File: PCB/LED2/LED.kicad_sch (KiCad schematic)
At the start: 29 parts, among them J1 Conn_01x03, J2 USB-C, U1 ESP32-PICO-MINI-02, U2 QR, U3 CH340X, U4 Barcode, U5 MD8942

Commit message: Started tracking
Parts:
- removed C4 (x2): 100nF, RevK:C_0402, symbol Device:C
- removed U1: ESP32-PICO-MINI-02, RevK:ESP32-PICO-MINI-02, symbol RevK:ESP32-PICO-MINI-02
- removed U2: QR, RevK:QR-LED, symbol RevK:QR
- removed U3: CH340X, RevK:CH340X, symbol RevK:CH340X
- added C2: 22uF, RevK:C_0402, symbol Device:C
- added C3: 1uF, RevK:C_0402, symbol Device:C
- added J2: Shelly, RevK:Shelly, symbol RevK:Shelly
- added U2: ESP32-S3-MINI-1, RevK:ESP32-S3-MINI-1, symbol RevK:ESP32-S3-MINI-1-N4R2
- C1: value 1uF -> 100nF
- J1: now left out of the parts list
- R1: value 10k -> 10K
- R10: value 40k2 -> 39k2
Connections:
- net +3V3: now also C1.1, C2.1, J2.3 (3V3), U2.3 (3V3)
- net B: now also U2.15 (GPIO11)
- net D+: now also U2.24 (GPIO20)
- net D-: now also U2.23 (GPIO19)
- net G: now also U2.13 (GPIO9)
- net GND: now also C1.2, C2.2, C3.2, J2.1 (GND), U2.1 (GND), U2.2 (GND), U2.42 (GND), U2.43 (GND), U2.46 (GND), U2.47 (GND), U2.48 (GND), U2.49 (GND), U2.50 (GND), U2.51 (GND), U2.52 (GND), U2.53 (GND), U2.54 (GND), U2.55 (GND), U2.56 (GND), U2.57 (GND), U2.58 (GND), U2.59 (GND), U2.60 (GND), U2.61 (GND), U2.62 (GND), U2.63 (GND), U2.64 (GND), U2.65 (GND); no longer C1.1
- net R: now also U2.14 (GPIO10)
- net EN: no longer names the net of R1.2
- net EN: now also C3.1, U2.45 (EN); no longer C1.2
- new net: J2.5 (Tx), U2.39 (GPIO43)
- new net: J2.2 (0), U2.4 (GPIO0)
- new net: J2.4 (Rx), U2.40 (GPIO44)
- no-connect marks 20 -> 1

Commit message: New S3
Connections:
- net LED: now also U2.12 (GPIO8)
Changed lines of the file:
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@@
+    )
+  )
+  (global_label "LED" (shape output) (at 35.56 68.58 180) (fields_autoplaced)
+    (effects (font (size 1.27 1.27)) (justify right))
+    (property "Intersheetrefs" "${INTERSHEET_REFS}" (at 29.7819 68.58 0)
+      (effects (font (size 1.27 1.27)) (justify right) hide)
     )
   )

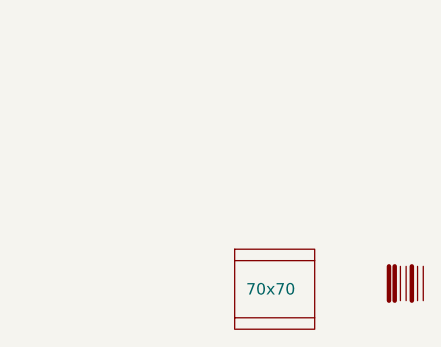
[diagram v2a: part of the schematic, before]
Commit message: LED input
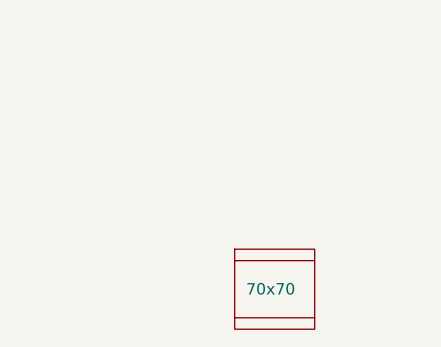
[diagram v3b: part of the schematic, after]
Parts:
- removed U4: Barcode, RevK:EAN-5060634238090, symbol RevK:Barcode
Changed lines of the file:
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@@
-    )
-  )
-  (symbol (lib_id "RevK:Barcode") (at 274.32 172.72 0) (unit 1)
-    (in_bom no) (on_board yes) (dnp no) (fields_autoplaced)
-    (property "Reference" "U4" (at 274.32 175.895 0)
-      (effects (font (size 1.27 1.27)) hide)
-    )
-    (property "Value" "Barcode" (at 274.32 177.8 0)
-      (effects (font (size 1.27 1.27)) hide)
-    )
-    (property "Footprint" "RevK:EAN-5060634238090" (at 273.685 173.355 0)
-      (effects (font (size 1.27 1.27)) hide)
-    )
-    (property "Datasheet" "" (at 273.685 173.355 0)
-      (effects (font (size 1.27 1.27)) hide)
-    )
-    (property "Note" "Non part, PCB printed" (at 274.32 167.005 0)
-      (effects (font (size 1.27 1.27)) hide)
-    )
-    (instances
-      (project "LED"
-        (path "/46c350bb-7de4-4e81-aafd-4af55e37aab0"
-          (reference "U4") (unit 1)
-        )
-      )
     )
   )

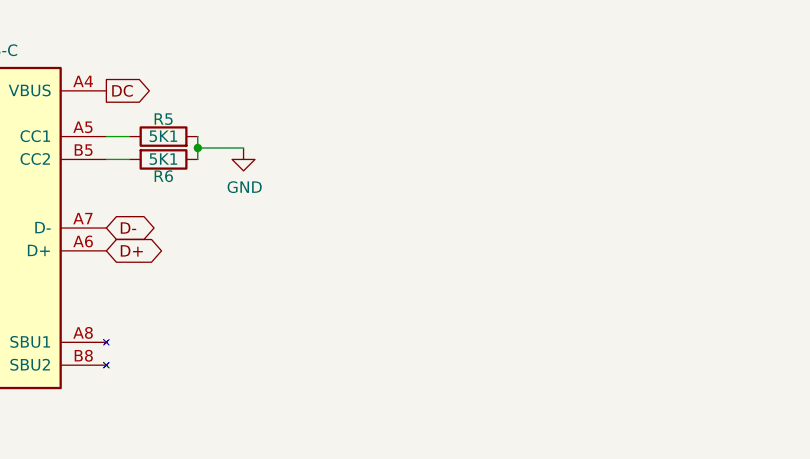
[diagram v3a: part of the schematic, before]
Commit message: Clean up, allow in panel USB prog.
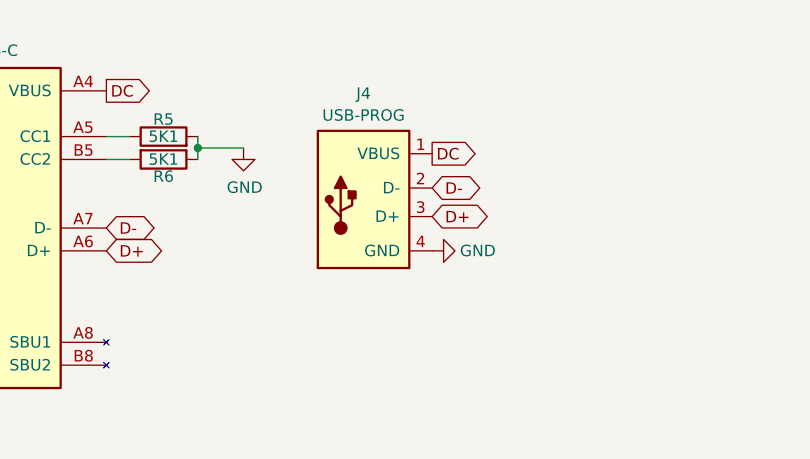
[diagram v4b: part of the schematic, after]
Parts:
- added J4: USB-PROG, RevK:USB-PROG, symbol RevK:USB-PROG
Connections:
- net D+: now also J4.3 (D+)
- net D-: now also J4.2 (D-)
- net DC: now also J4.1 (VBUS)
- net GND: now also J4.4 (GND)
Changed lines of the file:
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@@
+    )
+  )
+  (global_label "D-" (shape bidirectional) (at 209.55 37.465 0) (fields_autoplaced)
+    (effects (font (size 1.27 1.27)) (justify left))
+    (property "Intersheetrefs" "${INTERSHEET_REFS}" (at 215.5965 37.465 0)
+      (effects (font (size 1.27 1.27)) (justify left) hide)
     )
   )
@@
     )
   )
+  (global_label "DC" (shape input) (at 133.35 87.63 180) (fields_autoplaced)
+    (effects (font (size 1.27 1.27)) (justify right))
+    (property "Intersheetrefs" "${INTERSHEET_REFS}" (at 128.5584 87.63 0)
+      (effects (font (size 1.27 1.27)) (justify right) hide)
+    )
+  )
+  (global_label "DC" (shape output) (at 173.355 26.67 0) (fields_autoplaced)
+    (effects (font (size 1.27 1.27)) (justify left))
+    (property "Intersheetrefs" "${INTERSHEET_REFS}" (at 178.1466 26.67 0)
+      (effects (font (size 1.27 1.27)) (justify left) hide)
+    )
+  )
+  (global_label "R" (shape output) (at 35.56 73.66 180) (fields_autoplaced)
+    (effects (font (size 1.27 1.27)) (justify right))
+    (property "Intersheetrefs" "${INTERSHEET_REFS}" (at 31.959 73.66 0)
+      (effects (font (size 1.27 1.27)) (justify right) hide)
+    )
+  )
+  (global_label "DC" (shape input) (at 167.005 83.185 180) (fields_autoplaced)
+    (effects (font (size 1.27 1.27)) (justify right))
+    (property "Intersheetrefs" "${INTERSHEET_REFS}" (at 162.134 83.185 0)
+      (effects (font (size 1.27 1.27)) (justify right) hide)
+    )
+  )
+  (global_label "LED" (shape input) (at 113.03 90.17 180) (fields_autoplaced)
+    (effects (font (size 1.27 1.27)) (justify right))
+    (property "Intersheetrefs" "${INTERSHEET_REFS}" (at 107.2587 90.0906 0)
+      (effects (font (size 1.27 1.27)) (justify right) hide)
+    )
+  )
   (global_label "D-" (shape bidirectional) (at 173.355 41.91 0) (fields_autoplaced)
     (effects (font (size 1.27 1.27)) (justify left))
@@
     )
   )
-  (global_label "DC" (shape input) (at 133.35 87.63 180) (fields_autoplaced)
-    (effects (font (size 1.27 1.27)) (justify right))
-    (property "Intersheetrefs" "${INTERSHEET_REFS}" (at 128.5584 87.63 0)
-      (effects (font (size 1.27 1.27)) (justify right) hide)
-    )
-  )
-  (global_label "DC" (shape output) (at 173.355 26.67 0) (fields_autoplaced)
-    (effects (font (size 1.27 1.27)) (justify left))
-    (property "Intersheetrefs" "${INTERSHEET_REFS}" (at 178.1466 26.67 0)
-      (effects (font (size 1.27 1.27)) (justify left) hide)
-    )
-  )
-  (global_label "R" (shape output) (at 35.56 73.66 180) (fields_autoplaced)
-    (effects (font (size 1.27 1.27)) (justify right))
-    (property "Intersheetrefs" "${INTERSHEET_REFS}" (at 31.959 73.66 0)
-      (effects (font (size 1.27 1.27)) (justify right) hide)
-    )
-  )
-  (global_label "DC" (shape input) (at 167.005 83.185 180) (fields_autoplaced)
-    (effects (font (size 1.27 1.27)) (justify right))
-    (property "Intersheetrefs" "${INTERSHEET_REFS}" (at 162.134 83.185 0)
-      (effects (font (size 1.27 1.27)) (justify right) hide)
-    )
-  )
-  (global_label "LED" (shape input) (at 113.03 90.17 180) (fields_autoplaced)
-    (effects (font (size 1.27 1.27)) (justify right))
-    (property "Intersheetrefs" "${INTERSHEET_REFS}" (at 107.2587 90.0906 0)
-      (effects (font (size 1.27 1.27)) (justify right) hide)
-    )
-  )
   (global_label "G" (shape input) (at 100.33 41.275 180) (fields_autoplaced)
     (effects (font (size 1.27 1.27)) (justify right))
@@
     (property "Intersheetrefs" "${INTERSHEET_REFS}" (at 29.5135 96.52 0)
       (effects (font (size 1.27 1.27)) (justify right) hide)
+    )
+  )
+  (global_label "D+" (shape bidirectional) (at 209.55 40.64 0) (fields_autoplaced)
+    (effects (font (size 1.27 1.27)) (justify left))
+    (property "Intersheetrefs" "${INTERSHEET_REFS}" (at 215.5965 40.64 0)
+      (effects (font (size 1.27 1.27)) (justify left) hide)
+    )
+  )
+  (global_label "DC" (shape output) (at 209.55 33.655 0) (fields_autoplaced)
+    (effects (font (size 1.27 1.27)) (justify left))
+    (property "Intersheetrefs" "${INTERSHEET_REFS}" (at 214.3416 33.655 0)
+      (effects (font (size 1.27 1.27)) (justify left) hide)
     )
   )
@@
     )
   )
+  (symbol (lib_id "RevK:USB-PROG") (at 201.93 38.735 0) (unit 1)
+    (in_bom yes) (on_board yes) (dnp no) (fields_autoplaced)
+    (property "Reference" "J4" (at 201.93 26.9707 0)
+      (effects (font (size 1.27 1.27)))
+    )
+    (property "Value" "USB-PROG" (at 201.93 29.3949 0)
+      (effects (font (size 1.27 1.27)))
+    )
+    (property "Footprint" "RevK:USB-PROG" (at 205.74 40.005 0)
+      (effects (font (size 1.27 1.27)) hide)
+    )
+    (property "Datasheet" " ~" (at 205.74 40.005 0)
+      (effects (font (size 1.27 1.27)) hide)
+    )
+    (pin "1")
+    (pin "2")
+    (pin "3")
+    (pin "4")
+    (instances
+      (project "LED"
+        (path "/46c350bb-7de4-4e81-aafd-4af55e37aab0"
+          (reference "J4") (unit 1)
+        )
+      )
+    )
+  )
   (symbol (lib_id "Device:C") (at 53.975 31.115 0) (unit 1)
     (in_bom yes) (on_board yes) (dnp no) (fields_autoplaced)
@@
         )
       )
+    )
+  )
+  (symbol (lib_id "power:GND") (at 209.55 44.45 90) (unit 1)
+    (in_bom yes) (on_board yes) (dnp no)
+    (property "Reference" "#PWR01" (at 215.9 44.45 0)
+      (effects (font (size 1.27 1.27)) hide)
+    )
+    (property "Value" "GND" (at 214.63 44.45 90)
+      (effects (font (size 1.27 1.27)))
+    )
+    (property "Footprint" "" (at 209.55 44.45 0)
+      (effects (font (size 1.27 1.27)) hide)
+    )
+    (property "Datasheet" "" (at 209.55 44.45 0)
+      (effects (font (size 1.27 1.27)) hide)
+    )
+    (pin "1")
+    (instances
+      (project "LED"
+        (path "/46c350bb-7de4-4e81-aafd-4af55e37aab0"
+          (reference "#PWR01") (unit 1)
+        )
+      )

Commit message: New Reg
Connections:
- net GND: now also U2.10 (GPIO6), U2.11 (GPIO7), U2.5 (GPIO1), U2.6 (GPIO2), U2.8 (GPIO4), U2.9 (GPIO5)
- no-connect marks 1 -> 24
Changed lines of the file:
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@@
   (junction (at 80.01 105.41) (diameter 0) (color 0 0 0 0)
   )
+  (no_connect (at 66.04 96.52))
+  (no_connect (at 66.04 76.2))
+  (no_connect (at 66.04 101.6))
+  (no_connect (at 66.04 93.98))
+  (no_connect (at 35.56 91.44))
+  (no_connect (at 35.56 55.88))
+  (no_connect (at 35.56 101.6))
+  (no_connect (at 66.04 81.28))
+  (no_connect (at 35.56 88.9))
   (no_connect (at 167.005 93.98))
+  (no_connect (at 35.56 81.28))
+  (no_connect (at 66.04 86.36))
+  (no_connect (at 35.56 93.98))
+  (no_connect (at 66.04 78.74))
+  (no_connect (at 35.56 78.74))
+  (no_connect (at 66.04 73.66))
+  (no_connect (at 66.04 71.12))
+  (no_connect (at 66.04 66.04))
+  (no_connect (at 66.04 83.82))
+  (no_connect (at 35.56 83.82))
+  (no_connect (at 66.04 99.06))
+  (no_connect (at 66.04 88.9))
+  (no_connect (at 66.04 68.58))
+  (no_connect (at 35.56 86.36))
   (wire (pts (xy 183.515 33.02) (xy 183.515 34.29))
     (stroke (width 0) (type default))
@@
     )
   )
+  (symbol (lib_id "power:GND") (at 35.56 58.42 270) (unit 1)
+    (in_bom yes) (on_board yes) (dnp no) (fields_autoplaced)
+    (property "Reference" "#PWR0105" (at 29.21 58.42 0)
+      (effects (font (size 1.27 1.27)) hide)
+    )
+    (property "Value" "GND" (at 32.3851 58.42 90)
+      (effects (font (size 1.27 1.27)) (justify right))
+    )
+    (property "Footprint" "" (at 35.56 58.42 0)
+      (effects (font (size 1.27 1.27)) hide)
+    )
+    (property "Datasheet" "" (at 35.56 58.42 0)
+      (effects (font (size 1.27 1.27)) hide)
+    )
+    (pin "1")
+    (instances
+      (project "GenericS3"
+        (path "/2d210a96-f81f-42a9-8bf4-1b43c11086f3"
+          (reference "#PWR0105") (unit 1)
+        )
+      )
+      (project "LED"
+        (path "/46c350bb-7de4-4e81-aafd-4af55e37aab0"
+          (reference "#PWR04") (unit 1)
+        )
+      )
+    )
+  )
   (symbol (lib_id "RevK:Hidden") (at 199.39 92.075 0) (unit 1)
     (in_bom yes) (on_board yes) (dnp no)
@@
         (path "/46c350bb-7de4-4e81-aafd-4af55e37aab0"
           (reference "#PWR022") (unit 1)
+        )
+      )
+    )
+  )
+  (symbol (lib_id "power:GND") (at 35.56 63.5 270) (unit 1)
+    (in_bom yes) (on_board yes) (dnp no) (fields_autoplaced)
+    (property "Reference" "#PWR0105" (at 29.21 63.5 0)
+      (effects (font (size 1.27 1.27)) hide)
+    )
+    (property "Value" "GND" (at 32.3851 63.5 90)
+      (effects (font (size 1.27 1.27)) (justify right))
+    )
+    (property "Footprint" "" (at 35.56 63.5 0)
+      (effects (font (size 1.27 1.27)) hide)
+    )
+    (property "Datasheet" "" (at 35.56 63.5 0)
+      (effects (font (size 1.27 1.27)) hide)
+    )
+    (pin "1")
+    (instances
+      (project "GenericS3"
+        (path "/2d210a96-f81f-42a9-8bf4-1b43c11086f3"
+          (reference "#PWR0105") (unit 1)
+        )
+      )
+      (project "LED"
+        (path "/46c350bb-7de4-4e81-aafd-4af55e37aab0"
+          (reference "#PWR06") (unit 1)
         )
       )
@@
     )
   )
+  (symbol (lib_id "power:GND") (at 35.56 53.34 270) (unit 1)
+    (in_bom yes) (on_board yes) (dnp no) (fields_autoplaced)
+    (property "Reference" "#PWR0105" (at 29.21 53.34 0)
+      (effects (font (size 1.27 1.27)) hide)
+    )
+    (property "Value" "GND" (at 32.3851 53.34 90)
+      (effects (font (size 1.27 1.27)) (justify right))
+    )
+    (property "Footprint" "" (at 35.56 53.34 0)
+      (effects (font (size 1.27 1.27)) hide)
+    )
+    (property "Datasheet" "" (at 35.56 53.34 0)
+      (effects (font (size 1.27 1.27)) hide)
+    )
+    (pin "1")
+    (instances
+      (project "GenericS3"
+        (path "/2d210a96-f81f-42a9-8bf4-1b43c11086f3"
+          (reference "#PWR0105") (unit 1)
+        )
+      )
+      (project "LED"
+        (path "/46c350bb-7de4-4e81-aafd-4af55e37aab0"
+          (reference "#PWR03") (unit 1)
+        )
+      )
+    )
+  )
   (symbol (lib_name "GND_1") (lib_id "power:GND") (at 66.04 60.96 90) (unit 1)
     (in_bom yes) (on_board yes) (dnp no) (fields_autoplaced)
@@
         (path "/46c350bb-7de4-4e81-aafd-4af55e37aab0"
           (reference "C8") (unit 1)
+        )
+      )
+    )
+  )
+  (symbol (lib_id "power:GND") (at 35.56 50.8 270) (unit 1)
+    (in_bom yes) (on_board yes) (dnp no) (fields_autoplaced)
+    (property "Reference" "#PWR0105" (at 29.21 50.8 0)
+      (effects (font (size 1.27 1.27)) hide)
+    )
+    (property "Value" "GND" (at 32.3851 50.8 90)
+      (effects (font (size 1.27 1.27)) (justify right))
+    )
+    (property "Footprint" "" (at 35.56 50.8 0)
+      (effects (font (size 1.27 1.27)) hide)
+    )
+    (property "Datasheet" "" (at 35.56 50.8 0)
+      (effects (font (size 1.27 1.27)) hide)
+    )
+    (pin "1")
+    (instances
+      (project "GenericS3"
+        (path "/2d210a96-f81f-42a9-8bf4-1b43c11086f3"
+          (reference "#PWR0105") (unit 1)
+        )
+      )
+      (project "LED"
+        (path "/46c350bb-7de4-4e81-aafd-4af55e37aab0"
+          (reference "#PWR02") (unit 1)
         )
       )
@@
     )
   )
+  (symbol (lib_id "power:GND") (at 35.56 66.04 270) (unit 1)
+    (in_bom yes) (on_board yes) (dnp no) (fields_autoplaced)
+    (property "Reference" "#PWR0105" (at 29.21 66.04 0)
+      (effects (font (size 1.27 1.27)) hide)
+    )
+    (property "Value" "GND" (at 32.3851 66.04 90)
+      (effects (font (size 1.27 1.27)) (justify right))
+    )
+    (property "Footprint" "" (at 35.56 66.04 0)
+      (effects (font (size 1.27 1.27)) hide)
+    )
+    (property "Datasheet" "" (at 35.56 66.04 0)
+      (effects (font (size 1.27 1.27)) hide)
+    )
+    (pin "1")
+    (instances
+      (project "GenericS3"
+        (path "/2d210a96-f81f-42a9-8bf4-1b43c11086f3"
+          (reference "#PWR0105") (unit 1)
+        )
+      )
+      (project "LED"
+        (path "/46c350bb-7de4-4e81-aafd-4af55e37aab0"
+          (reference "#PWR07") (unit 1)
+        )
+      )
+    )
+  )
   (symbol (lib_id "RevK:VCUT") (at 259.715 176.53 0) (unit 1)
     (in_bom no) (on_board yes) (dnp no) (fields_autoplaced)
@@
         )
       )
+    )
+  )
+  (symbol (lib_id "power:GND") (at 35.56 60.96 270) (unit 1)
+    (in_bom yes) (on_board yes) (dnp no) (fields_autoplaced)
+    (property "Reference" "#PWR0105" (at 29.21 60.96 0)
+      (effects (font (size 1.27 1.27)) hide)
+    )
+    (property "Value" "GND" (at 32.3851 60.96 90)
+      (effects (font (size 1.27 1.27)) (justify right))
+    )
+    (property "Footprint" "" (at 35.56 60.96 0)
+      (effects (font (size 1.27 1.27)) hide)
+    )
+    (property "Datasheet" "" (at 35.56 60.96 0)
+      (effects (font (size 1.27 1.27)) hide)
+    )
+    (pin "1")
+    (instances
+      (project "GenericS3"
+        (path "/2d210a96-f81f-42a9-8bf4-1b43c11086f3"
+          (reference "#PWR0105") (unit 1)
+        )
+      )
+      (project "LED"
+        (path "/46c350bb-7de4-4e81-aafd-4af55e37aab0"
+          (reference "#PWR05") (unit 1)
+        )
+      )
